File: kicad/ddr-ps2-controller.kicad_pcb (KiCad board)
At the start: 2 copper layers, 100 x 40 mm, 73 parts, among them J1 BTN0, J2 BTN1, J3 BTN2, J4 BTN3, J5 ISCP, J6 PS2, J7 BTN4, J8 BTN5/UPSTREAM, Q1 DMN63D8LDW, U1 ATtiny20-MMH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

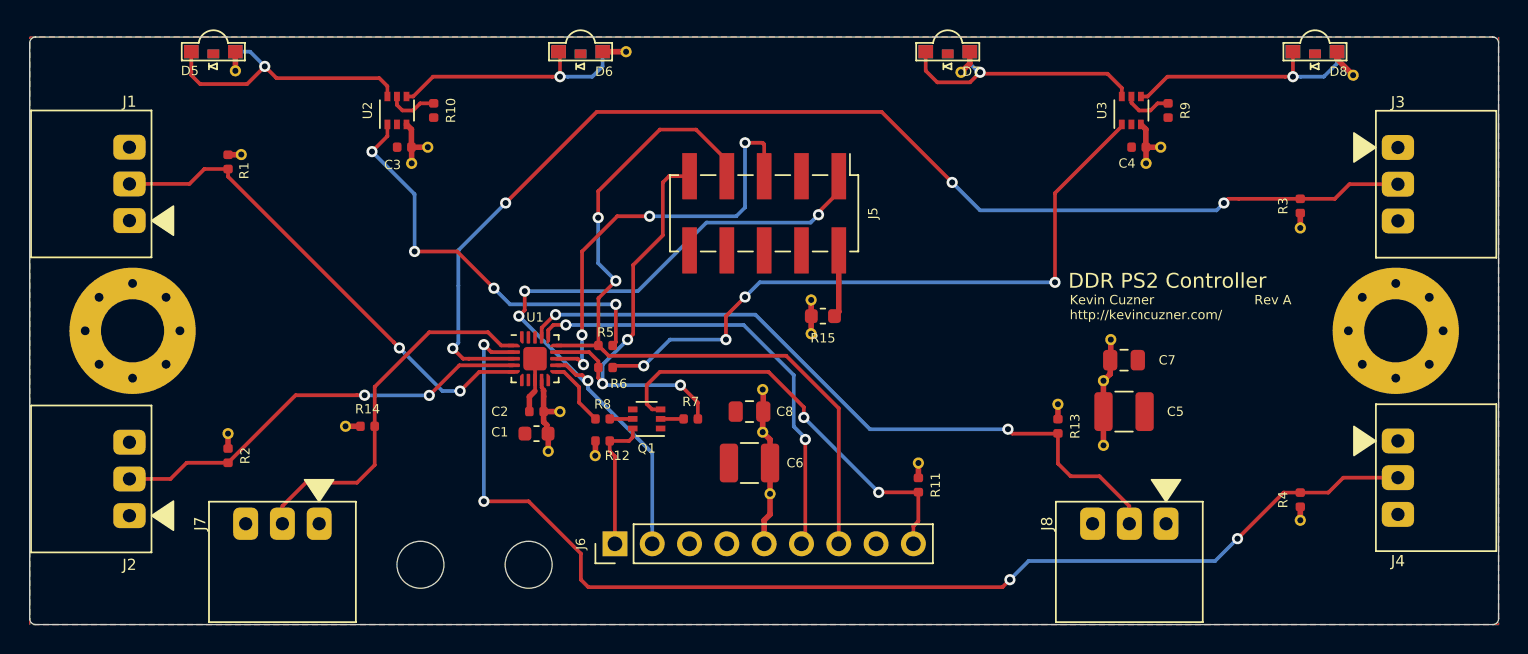
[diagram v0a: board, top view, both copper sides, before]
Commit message: Updating PCB and Schematic for rev B, fixing TPI and footprint issues
The programming interface for this microcontroller is TPI and for some
reason I wired it to be ISP. This implements a greenwire I did to work
around it.

I did not double-check the footprint for the SMD header. I've now added
the footprint from the datasheet.

Schematic library updated
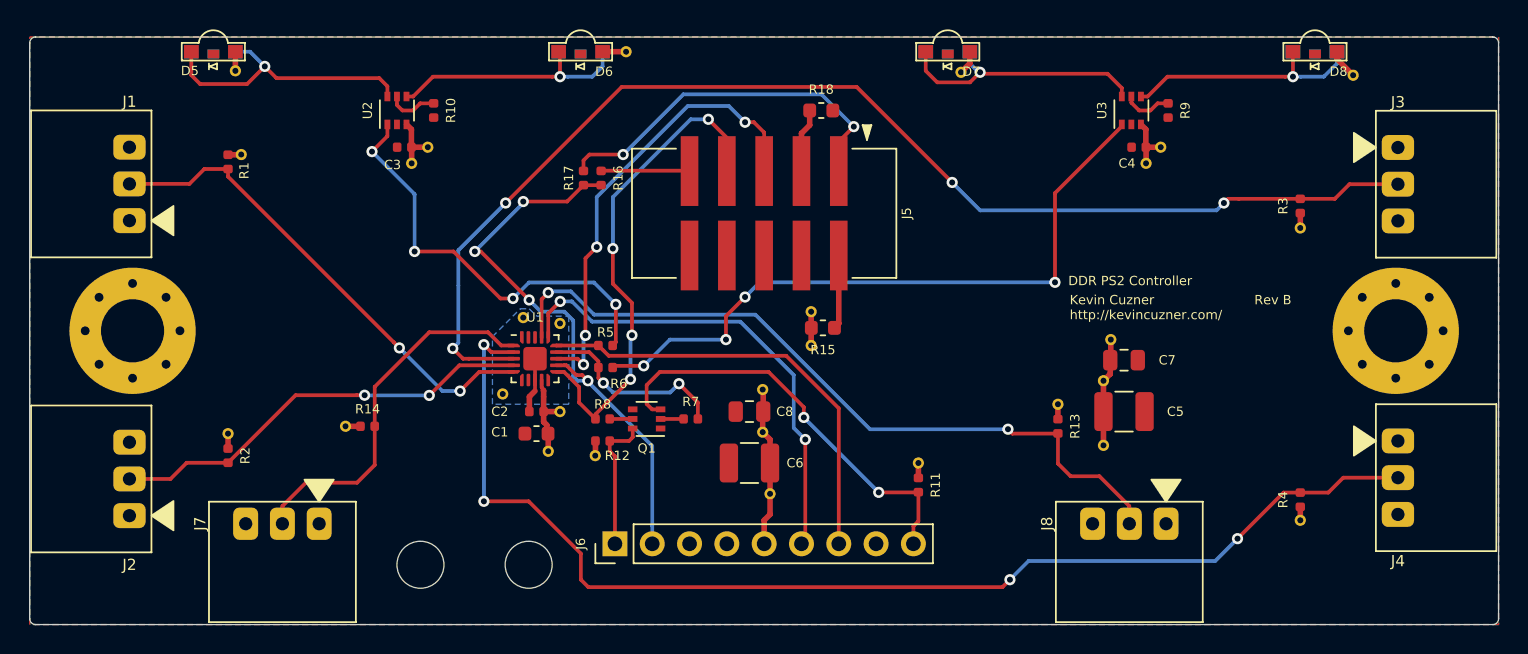
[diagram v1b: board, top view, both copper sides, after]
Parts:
- removed the REF** at (153.2, 100.2)
- removed the REF** at (153.2, 97.9)
- added R16: 1K, Resistor_SMD:R_0402_1005Metric, F.Cu at (138.9, 89.6)
- added R17: 0, Resistor_SMD:R_0402_1005Metric, F.Cu at (137.7, 89.6)
- added R18: 0, Resistor_SMD:R_0603_1608Metric, F.Cu at (153.9, 85.0)
- added REF**: 1PIN_VIA, ddr-ps2-controller:1PIN_VIA, F.Cu at (136.1, 99.5)
- added REF**: 1PIN_VIA, ddr-ps2-controller:1PIN_VIA, F.Cu at (133.6, 99.1)
- added REF**: 1PIN_VIA, ddr-ps2-controller:1PIN_VIA, F.Cu at (132.2, 104.3)
- added REF**: 1PIN_VIA, ddr-ps2-controller:1PIN_VIA, F.Cu at (153.2, 101.0)
- added REF**: 1PIN_VIA, ddr-ps2-controller:1PIN_VIA, F.Cu at (153.2, 98.7)
- J5: footprint Connector_PinHeader_2.54mm:PinHeader_2x05_P2.54mm_Vertical_SMD -> ddr-ps2-controller:CnC_3020_10_0300
- moved R15 0.80 mm to (154.0, 99.8)
- turned J5 to 180 degrees
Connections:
- J5 pad 1: /MOSI -> /ISP_MOSI
- J5 pad 3: GND -> Net-(J5-Pad3)
- J5 pad 7: /SCK -> /ACK
- J5 pad 9: /MISO -> /ISP_MISO
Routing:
- net /ACK: track 4.61 -> 34.2 mm, vias 0 -> 4
- net /ISP_MOSI: track 0.00 -> 25.3 mm, vias 0 -> 2
- net /SCK: track 54.2 -> 30.2 mm, vias 2 -> 0
- net /MISO: track 30.3 -> 13.3 mm, vias 3 -> 2
- net /MOSI: track 49.2 -> 39.6 mm
- net /ISP_MISO: track 0.00 -> 6.04 mm
- net Net-(J5-Pad3): track 0.00 -> 4.36 mm
- net /BTN5_UPSTREAM: track 48.8 -> 51.3 mm
- net /SS#: track 30.7 -> 32.7 mm
- net /RESET#: track 30.0 -> 31.5 mm
- net /BTN2: track 82.7 -> 84.1 mm
- net /LED_CTL0: track 28.4 -> 29.3 mm
- added copper zone on B.Cu, net GND
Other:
- board text added: "Rev B"
- board text removed: "Rev A"
